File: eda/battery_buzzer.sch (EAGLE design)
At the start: 19 parts, among them U1 ISL83491SOIC, U2 ATTINY1634

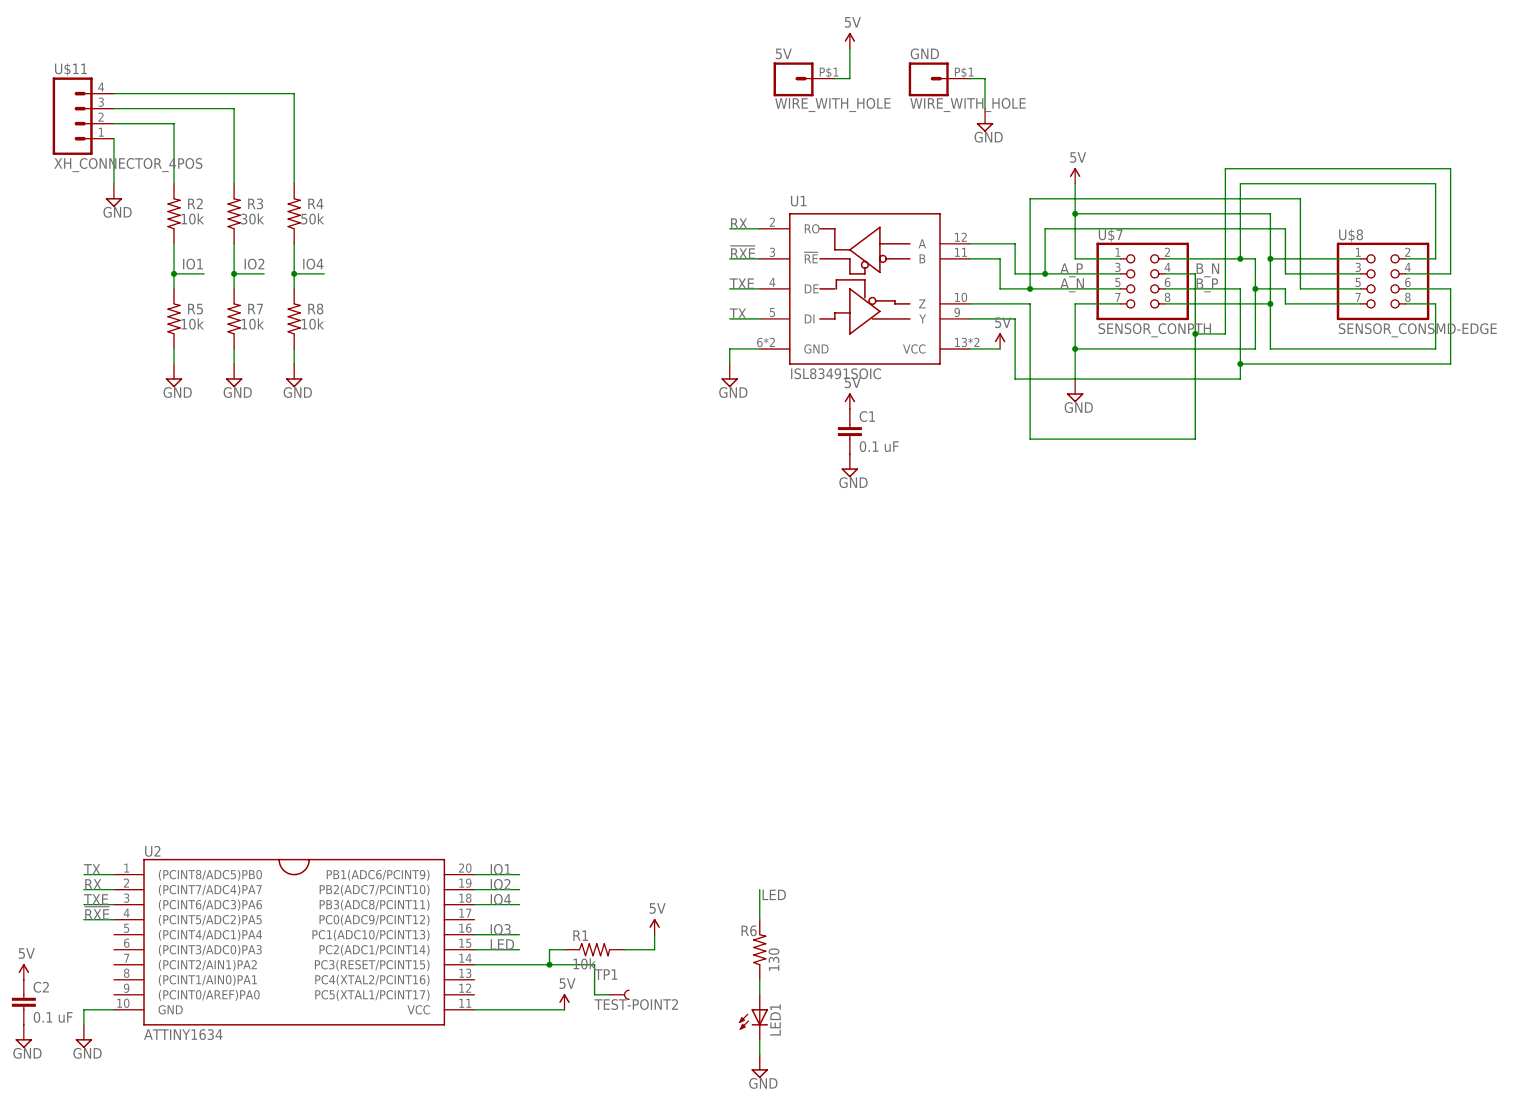
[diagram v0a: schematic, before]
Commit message: Minor fixes to battery_buzzer (sch and brd).
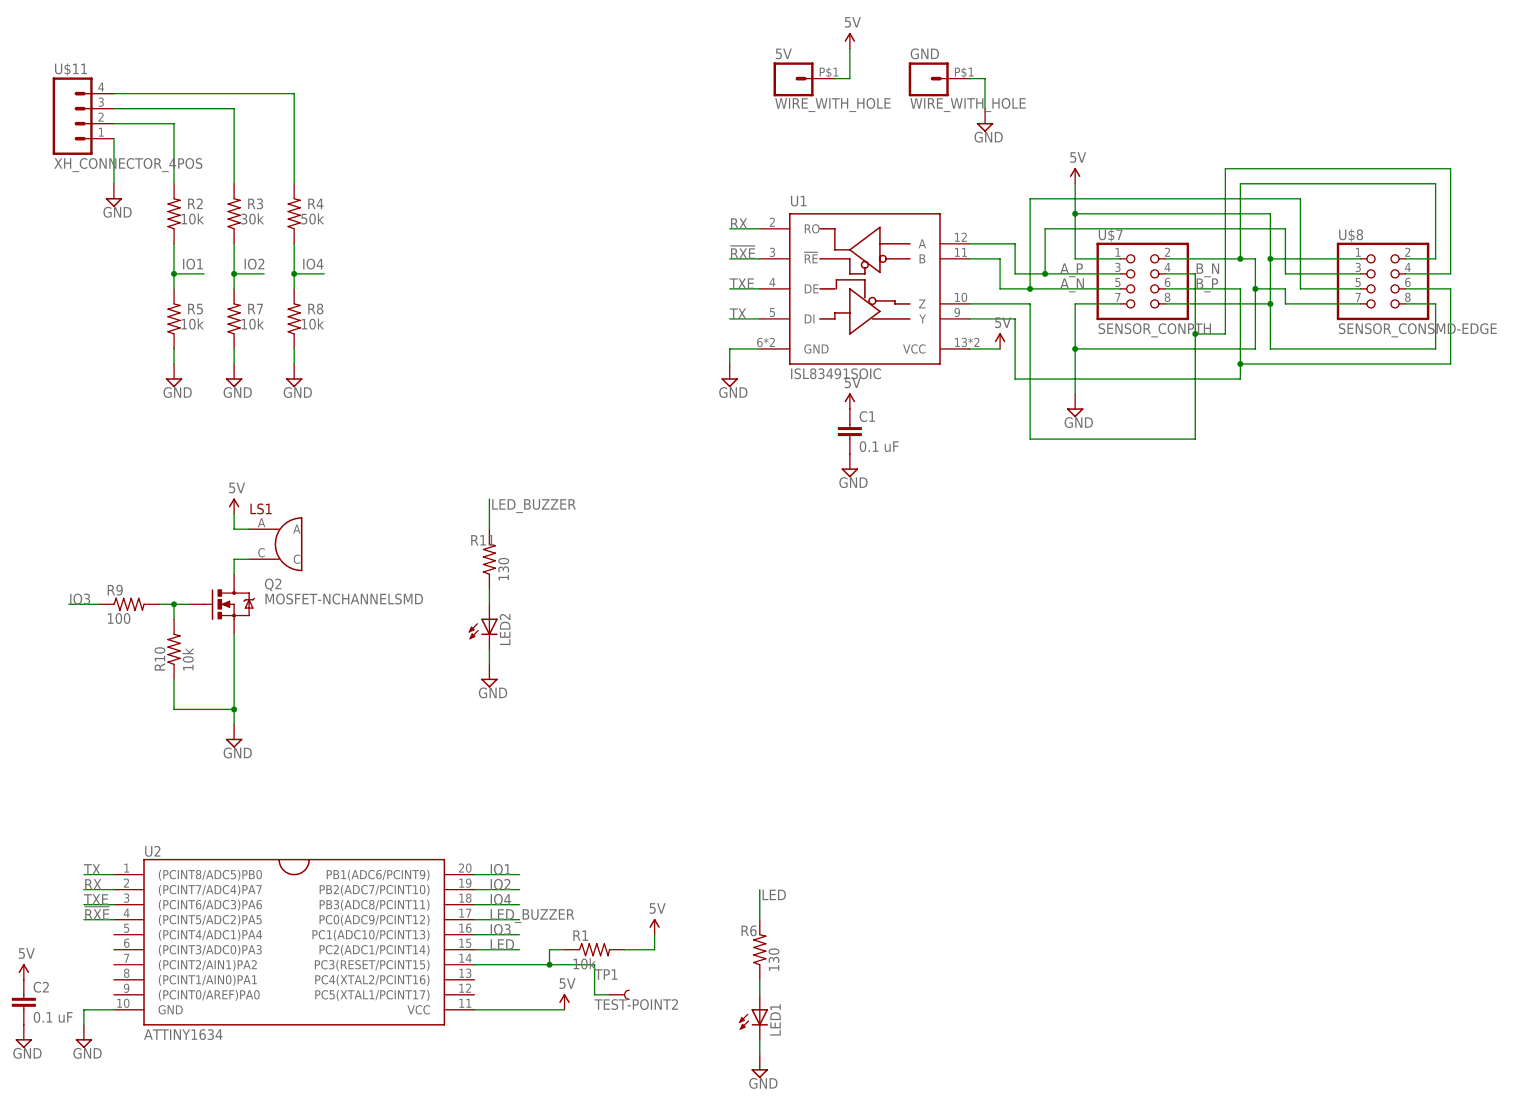
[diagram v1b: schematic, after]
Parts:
- added LED2: (no value), pie:LED0805
- added LS1: (no value), pie:BUZZER
- added Q2: MOSFET-NCHANNELSMD, pie:MOSFET-NCHANNELSMD
- added R10: 10k, pie:R-US_R0603
- added R11: 130, pie:R-US_R0603
- added R9: 100, pie:R-US_R0603
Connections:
- new net LED_BUZZER: R11.2, U2.PC0(ADC9/PCINT12)
- new net N$5: LS1.C, Q2.D
- new net N$6: Q2.G, R10.2, R9.2
- new net N$7: LED2.A, R11.1
- net 5V: now also LS1.A
- net GND: now also LED2.C, Q2.S, R10.1
- net IO3: now also R9.1
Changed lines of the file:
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@@
 <parts>
 <part name="FRAME1" library="pie" deviceset="FRAME-LETTER" device="">
-<attribute name="AUTHOR" value="Devin He"/>
+<attribute name="AUTHOR" value="Devin He, Krystyn Neisess"/>
 <attribute name="REVISION" value="A"/>
 </part>
@@
 <part name="SUPPLY9" library="pie" deviceset="GND" device=""/>
 <part name="SUPPLY10" library="pie" deviceset="GND" device=""/>
+<part name="LS1" library="pie" deviceset="BUZZER" device=""/>
+<part name="R9" library="pie" deviceset="R-US_" device="R0603" value="100"/>
+<part name="R10" library="pie" deviceset="R-US_" device="R0603" value="10k"/>
+<part name="U$12" library="pie" deviceset="5V" device=""/>
+<part name="SUPPLY11" library="pie" deviceset="GND" device=""/>
+<part name="R11" library="pie" deviceset="R-US_" device="R0603" value="130"/>
+<part name="LED2" library="pie" deviceset="LED" device="0805"/>
+<part name="SUPPLY13" library="pie" deviceset="GND" device=""/>
+<part name="Q2" library="pie" deviceset="MOSFET-NCHANNEL" device="SMD"/>
 </parts>
 <sheets>
@@
 <instance part="U$8" gate="G$1" x="236.22" y="139.7"/>
 <instance part="U$9" gate="G$1" x="182.88" y="154.94"/>
-<instance part="SUPPLY5" gate="GND" x="182.88" y="119.38"/>
+<instance part="SUPPLY5" gate="GND" x="182.88" y="116.84"/>
 <instance part="GND" gate="G$1" x="157.48" y="172.72"/>
 <instance part="5V" gate="G$1" x="134.62" y="172.72"/>
@@
 <instance part="SUPPLY9" gate="GND" x="40.64" y="121.92"/>
 <instance part="SUPPLY10" gate="GND" x="50.8" y="121.92"/>
+<instance part="LS1" gate="G$1" x="48.26" y="93.98"/>
+<instance part="R9" gate="G$1" x="22.86" y="83.82"/>
+<instance part="R10" gate="G$1" x="30.48" y="76.2" rot="R90"/>
+<instance part="U$12" gate="G$1" x="40.64" y="99.06"/>
+<instance part="SUPPLY11" gate="GND" x="40.64" y="60.96"/>
+<instance part="R11" gate="G$1" x="83.82" y="91.44" smashed="yes" rot="R90">
+<attribute name="NAME" x="80.518" y="95.5294" size="1.778" layer="95" rot="MR180"/>
+<attribute name="VALUE" x="87.122" y="87.63" size="1.778" layer="96" rot="R90"/>
+</instance>
+<instance part="LED2" gate="G$1" x="83.82" y="78.74"/>
+<instance part="SUPPLY13" gate="GND" x="83.82" y="71.12"/>
+<instance part="Q2" gate="G$1" x="40.64" y="83.82"/>
 </instances>
 <busses>
@@
 <pinref part="5V" gate="G$1" pin="2"/>
 </segment>
+<segment>
+<pinref part="LS1" gate="G$1" pin="A"/>
+<pinref part="U$12" gate="G$1" pin="5V"/>
+<wire x1="43.18" y1="96.52" x2="40.64" y2="96.52" width="0.1524" layer="91"/>
+<wire x1="40.64" y1="96.52" x2="40.64" y2="99.06" width="0.1524" layer="91"/>
+</segment>
 </net>
 <net name="GND" class="0">
@@
 <wire x1="182.88" y1="134.62" x2="182.88" y2="127" width="0.1524" layer="91"/>
 <pinref part="U$7" gate="G$1" pin="2"/>
-<wire x1="182.88" y1="127" x2="182.88" y2="121.92" width="0.1524" layer="91"/>
+<wire x1="182.88" y1="127" x2="182.88" y2="119.38" width="0.1524" layer="91"/>
 <wire x1="198.12" y1="142.24" x2="210.82" y2="142.24" width="0.1524" layer="91"/>
 <wire x1="210.82" y1="142.24" x2="213.36" y2="142.24" width="0.1524" layer="91"/>
@@
 <pinref part="SUPPLY7" gate="GND" pin="GND"/>
 </segment>
+<segment>
+<wire x1="40.64" y1="63.5" x2="40.64" y2="66.04" width="0.1524" layer="91"/>
+<pinref part="SUPPLY11" gate="GND" pin="GND"/>
+<wire x1="40.64" y1="66.04" x2="40.64" y2="78.74" width="0.1524" layer="91"/>
+<wire x1="30.48" y1="66.04" x2="40.64" y2="66.04" width="0.1524" layer="91"/>
+<junction x="40.64" y="66.04"/>
+<pinref part="Q2" gate="G$1" pin="S"/>
+<pinref part="R10" gate="G$1" pin="1"/>
+<wire x1="30.48" y1="71.12" x2="30.48" y2="66.04" width="0.1524" layer="91"/>
+</segment>
+<segment>
+<pinref part="LED2" gate="G$1" pin="C"/>
+<pinref part="SUPPLY13" gate="GND" pin="GND"/>
+<wire x1="83.82" y1="76.2" x2="83.82" y2="73.66" width="0.1524" layer="91"/>
+</segment>
 </net>
 <net name="TX" class="0">
@@
 <label x="83.82" y="27.94" size="1.778" layer="95"/>
 </segment>
+<segment>
+<pinref part="R9" gate="G$1" pin="1"/>
+<wire x1="17.78" y1="83.82" x2="12.7" y2="83.82" width="0.1524" layer="91"/>
+<label x="12.7" y="83.82" size="1.778" layer="95"/>
+</segment>
 </net>
 <net name="IO4" class="0">
@@
 </segment>
 </net>
+<net name="N$6" class="0">
+<segment>
+<pinref part="R9" gate="G$1" pin="2"/>
+<wire x1="33.02" y1="83.82" x2="30.48" y2="83.82" width="0.1524" layer="91"/>
+<pinref part="R10" gate="G$1" pin="2"/>
+<wire x1="30.48" y1="83.82" x2="27.94" y2="83.82" width="0.1524" layer="91"/>
+<wire x1="30.48" y1="81.28" x2="30.48" y2="83.82" width="0.1524" layer="91"/>
+<junction x="30.48" y="83.82"/>
+<pinref part="Q2" gate="G$1" pin="G"/>
+</segment>
+</net>
+<net name="N$5" class="0">
+<segment>
+<wire x1="40.64" y1="88.9" x2="40.64" y2="91.44" width="0.1524" layer="91"/>
+<pinref part="LS1" gate="G$1" pin="C"/>
+<wire x1="40.64" y1="91.44" x2="43.18" y2="91.44" width="0.1524" layer="91"/>
+<pinref part="Q2" gate="G$1" pin="D"/>
+</segment>
+</net>
+<net name="N$7" class="0">
+<segment>
+<pinref part="R11" gate="G$1" pin="1"/>
+<wire x1="83.82" y1="86.36" x2="83.82" y2="83.82" width="0.1524" layer="91"/>
+<pinref part="LED2" gate="G$1" pin="A"/>
+</segment>
+</net>
+<net name="LED_BUZZER" class="0">
+<segment>
+<wire x1="83.82" y1="101.6" x2="83.82" y2="96.52" width="0.1524" layer="91"/>
+<label x="84.074" y="99.822" size="1.778" layer="95"/>
+<pinref part="R11" gate="G$1" pin="2"/>
+</segment>
+<segment>
+<pinref part="U2" gate="G$1" pin="PC0(ADC9/PCINT12)"/>
+<wire x1="81.28" y1="30.48" x2="88.9" y2="30.48" width="0.1524" layer="91"/>
+<label x="83.82" y="30.48" size="1.778" layer="95"/>
+</segment>
+</net>

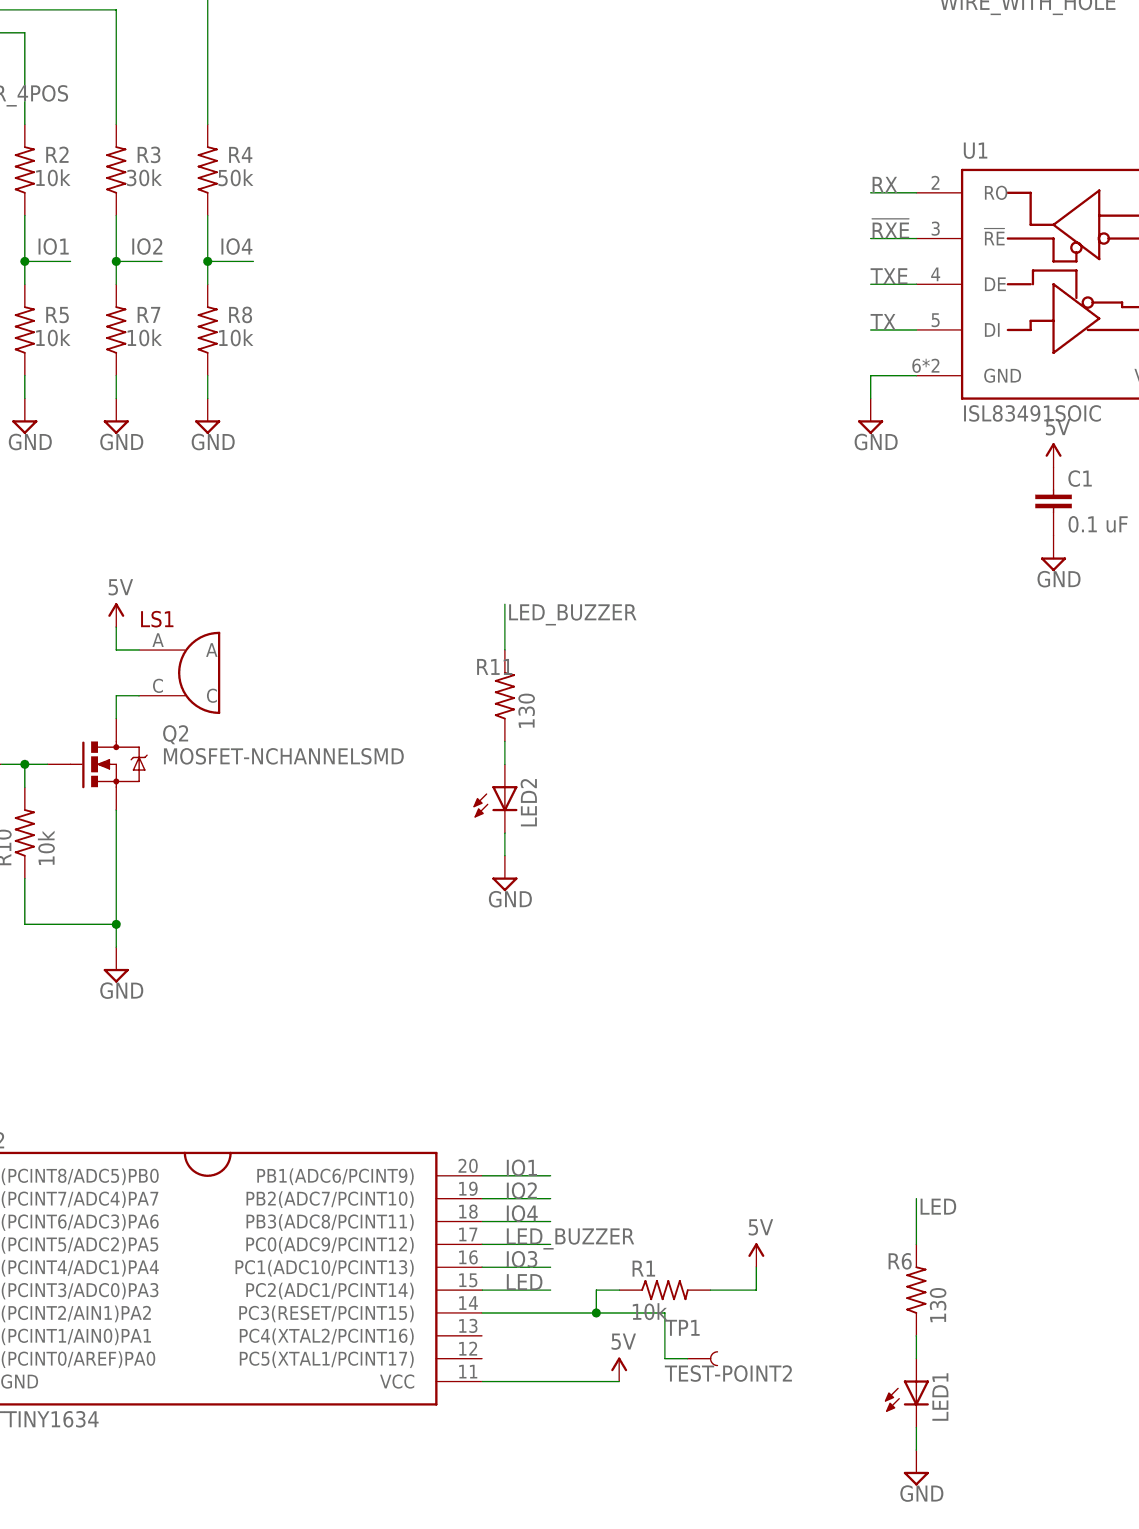
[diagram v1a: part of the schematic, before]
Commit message: All BOM metadata for explicit parts added
Changed C4 on Grizzly to 1206 and moved around parts so that plane
is not interrupted as much.

Smartsensor filter permutations are not embedded in the BOM metadata
and will be documented elsewhere.
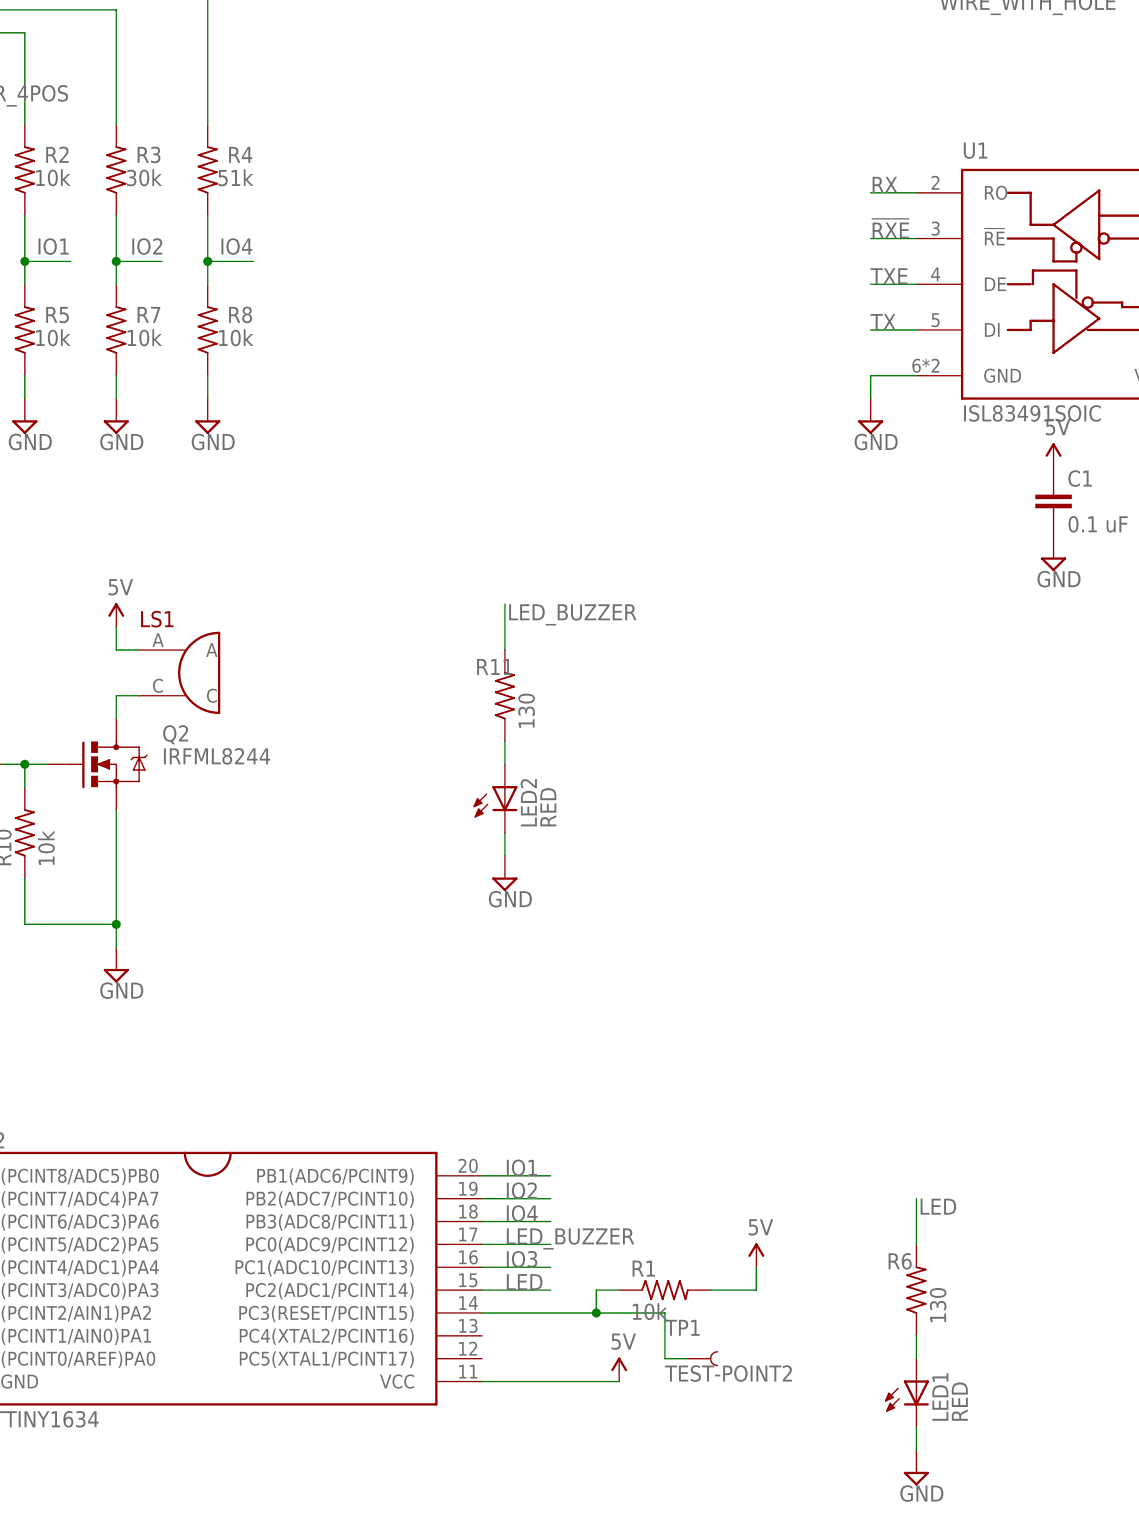
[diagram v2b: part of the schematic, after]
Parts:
- LED1, LED2: value (none) -> RED
- Q2: value MOSFET-NCHANNELSMD -> IRFML8244
- R4: value 50k -> 51k
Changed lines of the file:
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@@
 <setting verticaltext="up"/>
 </settings>
-<grid distance="0.1" unitdist="inch" unit="inch" style="lines" multiple="1" display="no" altdistance="0.01" altunitdist="inch" altunit="inch"/>
+<grid distance="0.1" unitdist="inch" unit="inch" style="lines" multiple="1" display="yes" altdistance="0.05" altunitdist="inch" altunit="inch"/>
 <layers>
 <layer number="1" name="Top" color="4" fill="1" visible="no" active="no"/>
@@
 <part name="TP1" library="pie" deviceset="TEST-POINT" device="2"/>
 <part name="R6" library="pie" deviceset="R-US_" device="R0603" value="130"/>
-<part name="LED1" library="pie" deviceset="LED" device="0805"/>
+<part name="LED1" library="pie" deviceset="LED" device="0805" value="RED"/>
 <part name="SUPPLY12" library="pie" deviceset="GND" device=""/>
 <part name="U$11" library="pie" deviceset="XH_CONNECTOR_4POS" device=""/>
 <part name="R2" library="pie" deviceset="R-US_" device="R0603" value="10k"/>
 <part name="R3" library="pie" deviceset="R-US_" device="R0603" value="30k"/>
-<part name="R4" library="pie" deviceset="R-US_" device="R0603" value="50k"/>
+<part name="R4" library="pie" deviceset="R-US_" device="R0603" value="51k"/>
 <part name="R5" library="pie" deviceset="R-US_" device="R0603" value="10k"/>
 <part name="R7" library="pie" deviceset="R-US_" device="R0603" value="10k"/>
@@
 <part name="SUPPLY11" library="pie" deviceset="GND" device=""/>
 <part name="R11" library="pie" deviceset="R-US_" device="R0603" value="130"/>
-<part name="LED2" library="pie" deviceset="LED" device="0805"/>
+<part name="LED2" library="pie" deviceset="LED" device="0805" value="RED"/>
 <part name="SUPPLY13" library="pie" deviceset="GND" device=""/>
-<part name="Q2" library="pie" deviceset="MOSFET-NCHANNEL" device="SMD"/>
+<part name="Q2" library="pie" deviceset="MOSFET-NCHANNEL" device="SMD" value="IRFML8244"/>
 </parts>
 <sheets>
